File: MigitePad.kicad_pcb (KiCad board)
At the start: 2 copper layers, 139.7 x 134.1 mm, 74 parts, among them J1 OLED, J2 LED-Lily58-cache, SW1 SW_Push, SW2 Rotary_Encoder_Switch, U1 ProMicro

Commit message: Rewired Encoder
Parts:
- added H9: MountingHole, Lily58-footprint:HOLE_M2_TH, F.Cu at (142.1, 60.2)
- moved H6 9.22 mm to (116.7, 124.3)
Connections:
- D31 pad 1: ROW1 -> ROW0
- SW2 pad S2: COL6 -> COL3
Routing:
- net ROW0: track 90.8 -> 155.3 mm, vias 0 -> 5
- net COL3: track 115.7 -> 166.2 mm, vias 0 -> 3
- net COL6: track 171.5 -> 151.0 mm, vias 2 -> 1
- net ROW1: track 208.9 -> 206.2 mm

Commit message: Gerbers and final touches
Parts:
- added G***: LOGO, Logo:MigiteLogo, F.Cu at (132.5, 104.3)

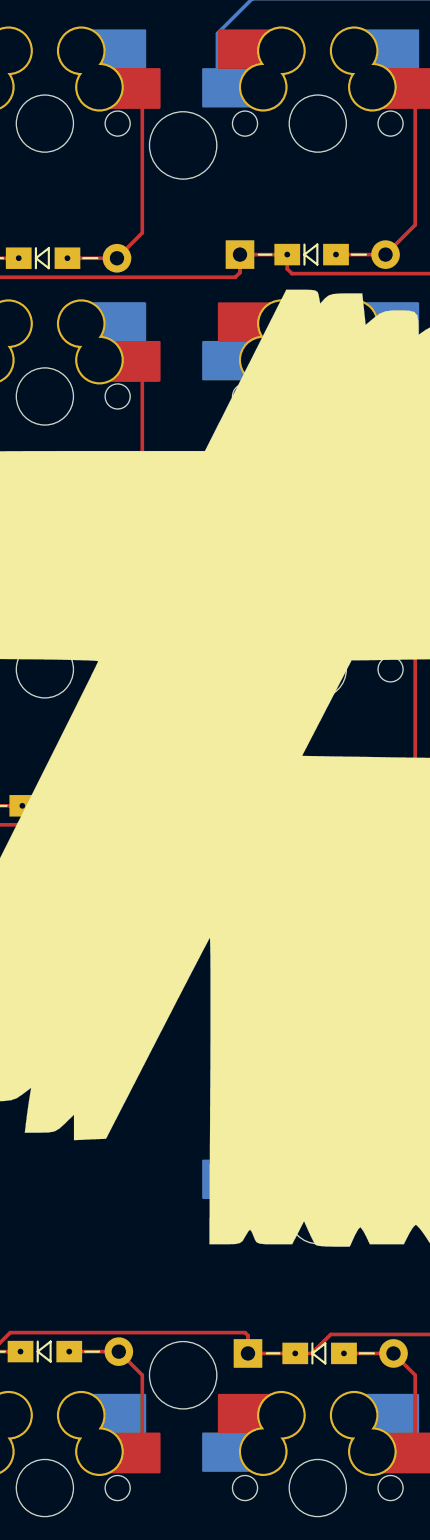
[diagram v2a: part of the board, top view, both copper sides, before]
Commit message: Corrected Col1 Trace
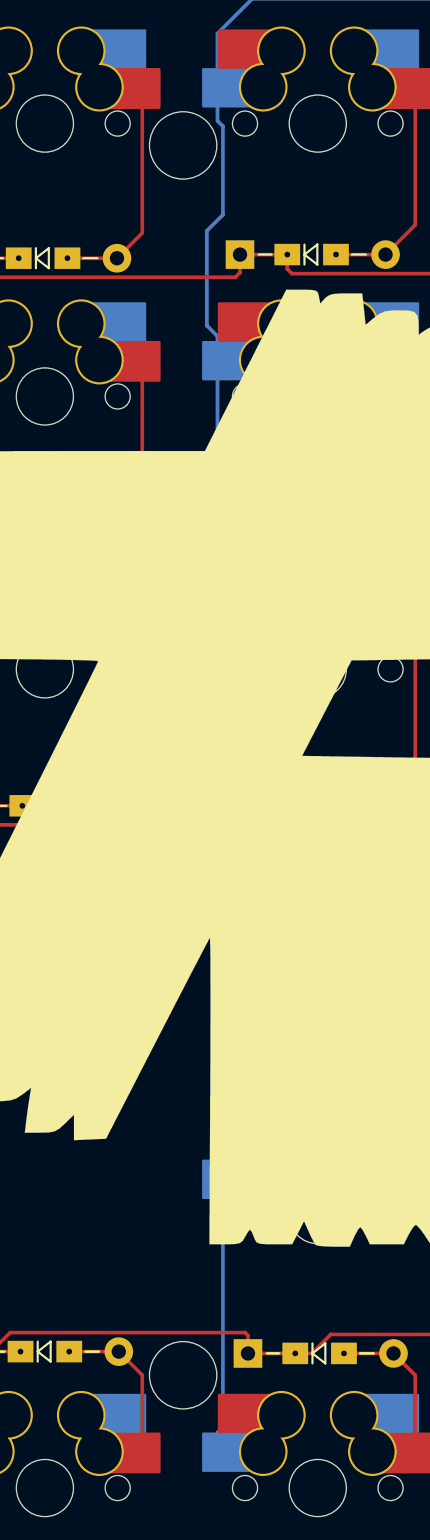
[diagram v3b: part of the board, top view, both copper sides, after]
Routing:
- net COL1: track 67.6 -> 164.1 mm
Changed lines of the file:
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@@
     (thickness 1.6)
     (drawings 22)
-    (tracks 552)
+    (tracks 568)
     (zones 0)
     (modules 76)
@@
     (35 F.Paste user hide)
     (36 B.SilkS user)
-    (37 F.SilkS user)
+    (37 F.SilkS user hide)
     (38 B.Mask user)
     (39 F.Mask user)
@@
   (segment (start 88.011 50.84402) (end 122.899047 50.84402) (width 0.254) (layer B.Cu) (net 37))
   (segment (start 122.899047 50.84402) (end 123.165 50.578066) (width 0.254) (layer B.Cu) (net 37))
+  (segment (start 85.583 57.063) (end 85.583 59.374742) (width 0.254) (layer B.Cu) (net 37))
+  (segment (start 85.962201 59.753943) (end 85.962201 65.929799) (width 0.254) (layer B.Cu) (net 37))
+  (segment (start 85.583 59.374742) (end 85.962201 59.753943) (width 0.254) (layer B.Cu) (net 37))
+  (segment (start 85.962201 65.929799) (end 84.836 67.056) (width 0.254) (layer B.Cu) (net 37))
+  (segment (start 84.836 67.056) (end 84.836 73.66) (width 0.254) (layer B.Cu) (net 37))
+  (segment (start 85.583 74.407) (end 85.583 76.113) (width 0.254) (layer B.Cu) (net 37))
+  (segment (start 84.836 73.66) (end 85.583 74.407) (width 0.254) (layer B.Cu) (net 37))
+  (segment (start 85.583 77.488) (end 85.583 95.163) (width 0.254) (layer B.Cu) (net 37))
+  (segment (start 85.583 76.113) (end 85.583 77.488) (width 0.254) (layer B.Cu) (net 37))
+  (segment (start 85.583 96.538) (end 85.583 133.263) (width 0.254) (layer B.Cu) (net 37))
+  (segment (start 85.583 95.163) (end 85.583 96.538) (width 0.254) (layer B.Cu) (net 37))
+  (segment (start 85.583 150.938) (end 85.583 152.313) (width 0.254) (layer B.Cu) (net 37))
+  (segment (start 85.962201 150.558799) (end 85.583 150.938) (width 0.254) (layer B.Cu) (net 37))
+  (segment (start 85.583 134.638) (end 85.962201 135.017201) (width 0.254) (layer B.Cu) (net 37))
+  (segment (start 85.962201 135.017201) (end 85.962201 150.558799) (width 0.254) (layer B.Cu) (net 37))
+  (segment (start 85.583 133.263) (end 85.583 134.638) (width 0.254) (layer B.Cu) (net 37))
   (segment (start 104.633 57.063) (end 104.633 152.313) (width 0.254) (layer B.Cu) (net 38))
   (segment (start 140.60173 40.27802) (end 144.81175 36.068) (width 0.254) (layer B.Cu) (net 38))

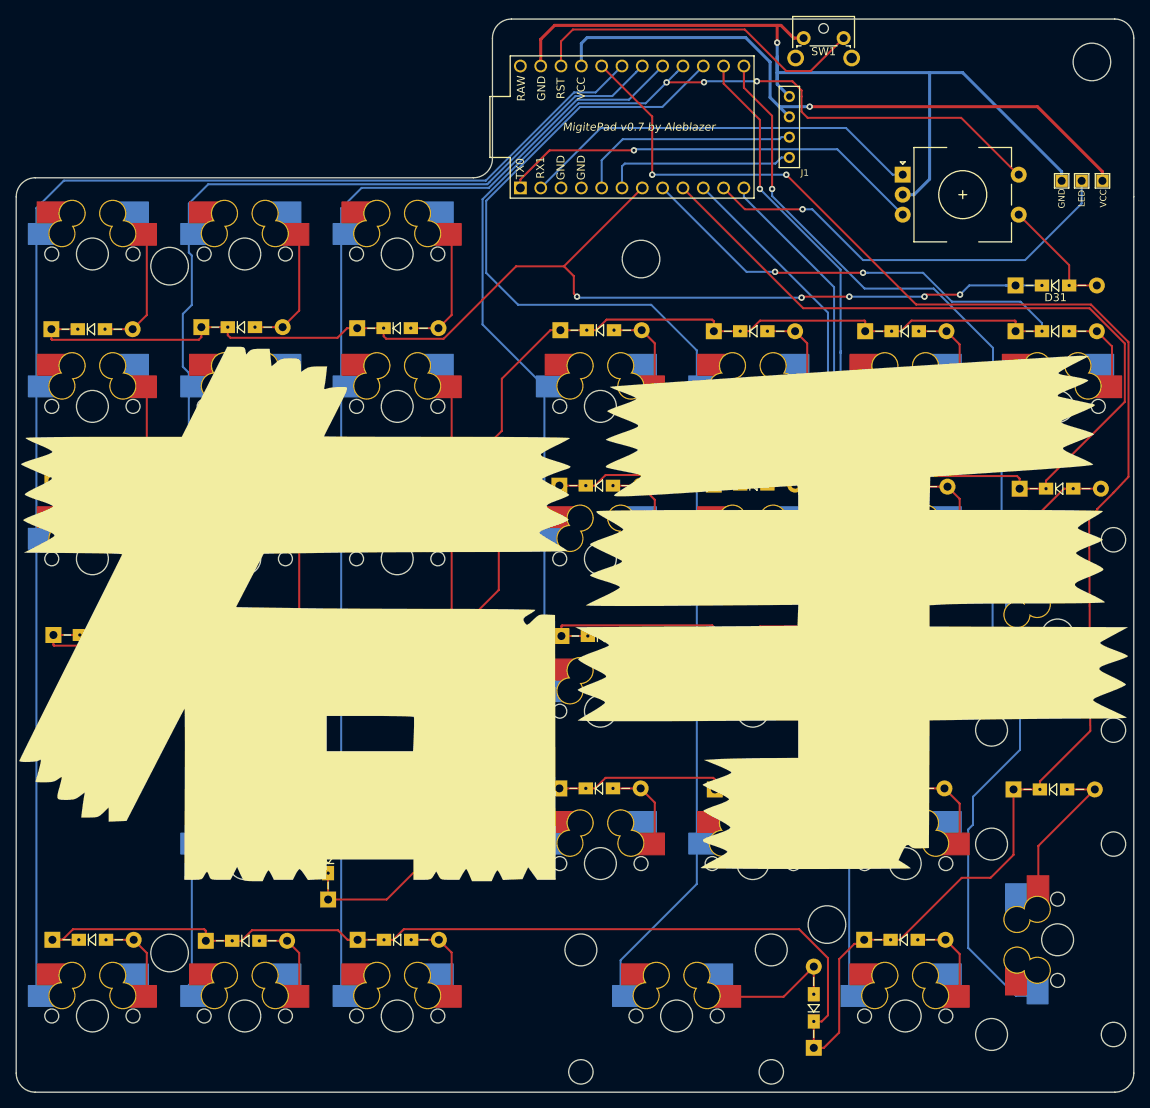
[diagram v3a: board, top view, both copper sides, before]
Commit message: Removed old Gerbers, fixed more traces
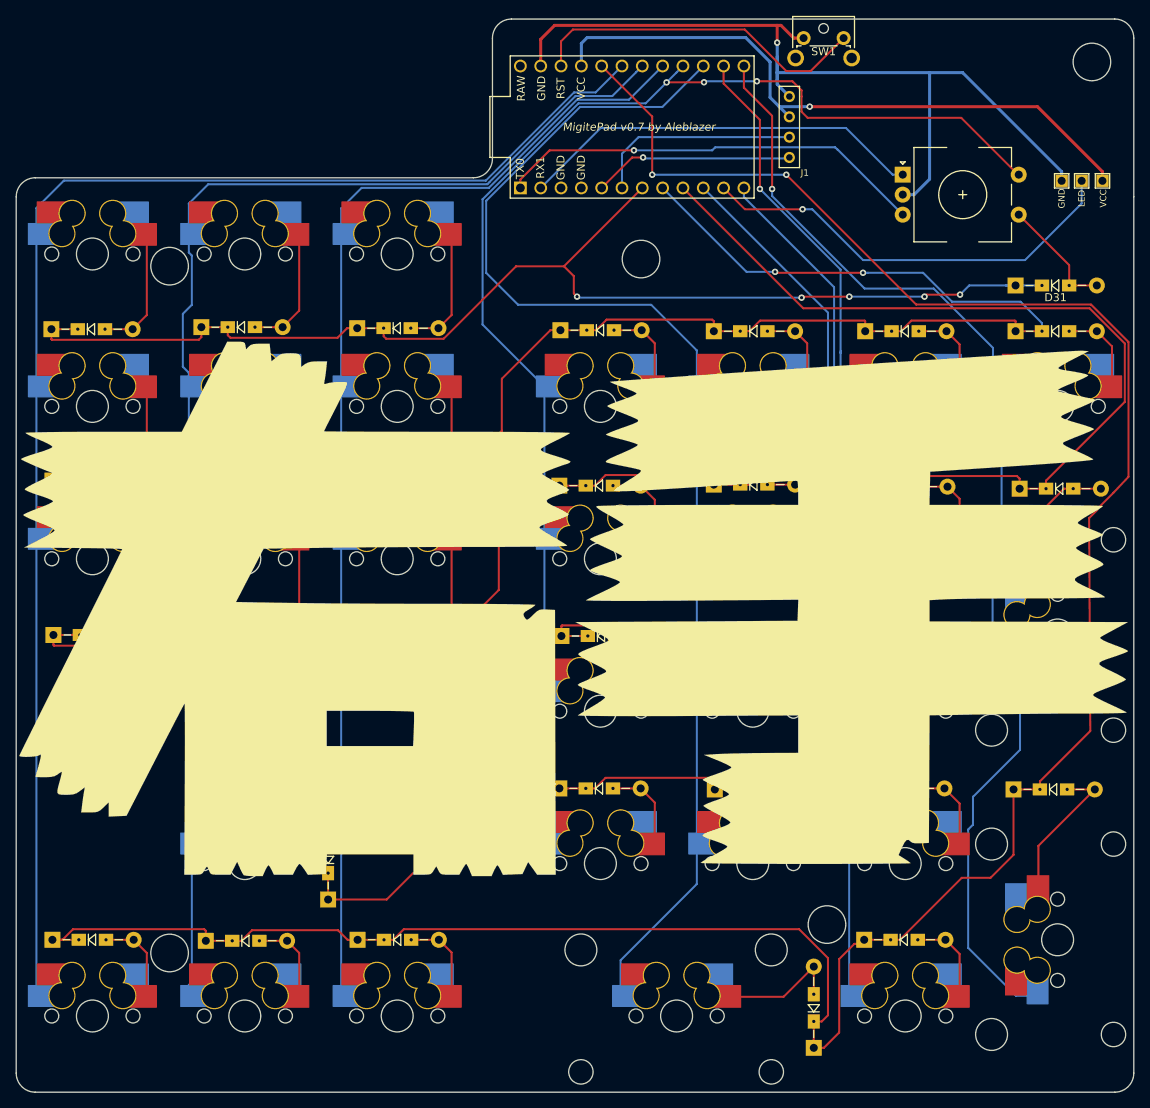
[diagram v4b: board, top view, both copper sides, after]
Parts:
- moved G*** 0.63 mm to (132.5, 103.6)
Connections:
- U1 pad 5: SCL -> SDA
- U1 pad 6: SDA -> SCL
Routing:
- net SCL: track 28.1 -> 26.1 mm
- net SDA: track 24.1 -> 25.2 mm, vias 0 -> 1
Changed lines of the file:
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@@
     (thickness 1.6)
     (drawings 22)
-    (tracks 568)
+    (tracks 572)
     (zones 0)
     (modules 76)
@@
     (35 F.Paste user hide)
     (36 B.SilkS user)
-    (37 F.SilkS user hide)
+    (37 F.SilkS user)
     (38 B.Mask user)
     (39 F.Mask user)
@@
   )
   (module Logo:MigiteLogo (layer F.Cu)
-    (at 132.461 104.267)
+    (at 132.461 103.632)
     (fp_text reference G*** (at 0 0) (layer F.SilkS) hide
       (effects (font (size 1.524 1.524) (thickness 0.3)))
@@
       (net 2 ROW0))
     (pad 6 thru_hole circle (at -1.27 7.62) (size 1.6 1.6) (drill 1.1) (layers *.Cu *.Mask F.SilkS)
-      (net 48 SDA))
-    (pad 5 thru_hole circle (at -3.81 7.62) (size 1.6 1.6) (drill 1.1) (layers *.Cu *.Mask F.SilkS)
       (net 47 SCL))
+    (pad 5 thru_hole circle (at -3.81 7.62) (size 1.6 1.6) (drill 1.1) (layers *.Cu *.Mask F.SilkS)
+      (net 48 SDA))
     (pad 4 thru_hole circle (at -6.35 7.62) (size 1.6 1.6) (drill 1.1) (layers *.Cu *.Mask F.SilkS)
       (net 45 GND))
@@
   (segment (start 191.663 41.148) (end 199.791 49.276) (width 0.381) (layer F.Cu) (net 46))
   (segment (start 163.195 41.148) (end 191.663 41.148) (width 0.381) (layer F.Cu) (net 46))
-  (segment (start 159.667172 44.958) (end 159.413172 45.212) (width 0.254) (layer B.Cu) (net 47))
-  (segment (start 160.655 44.958) (end 159.667172 44.958) (width 0.254) (layer B.Cu) (net 47))
-  (segment (start 159.413172 45.212) (end 139.827 45.212) (width 0.254) (layer B.Cu) (net 47))
-  (segment (start 137.19175 47.84725) (end 137.19175 51.308) (width 0.254) (layer B.Cu) (net 47))
-  (segment (start 139.827 45.212) (end 137.19175 47.84725) (width 0.254) (layer B.Cu) (net 47))
-  (segment (start 140.081 48.26) (end 139.73175 48.60925) (width 0.254) (layer B.Cu) (net 48))
-  (segment (start 158.905172 48.26) (end 140.081 48.26) (width 0.254) (layer B.Cu) (net 48))
-  (segment (start 160.655 47.498) (end 159.667172 47.498) (width 0.254) (layer B.Cu) (net 48))
-  (segment (start 139.73175 48.60925) (end 139.73175 51.308) (width 0.254) (layer B.Cu) (net 48))
-  (segment (start 159.667172 47.498) (end 158.905172 48.26) (width 0.254) (layer B.Cu) (net 48))
+  (segment (start 139.73175 47.025288) (end 139.73175 50.17663) (width 0.254) (layer B.Cu) (net 47))
+  (segment (start 141.799038 44.958) (end 139.73175 47.025288) (width 0.254) (layer B.Cu) (net 47))
+  (segment (start 139.73175 50.17663) (end 139.73175 51.308) (width 0.254) (layer B.Cu) (net 47))
+  (segment (start 160.655 44.958) (end 141.799038 44.958) (width 0.254) (layer B.Cu) (net 47))
+  (segment (start 160.655 47.498) (end 160.655 47.625) (width 0.254) (layer B.Cu) (net 48))
+  (segment (start 160.655 47.625) (end 142.494 47.625) (width 0.254) (layer B.Cu) (net 48))
+  (via (at 142.367 47.498) (size 0.8) (drill 0.4) (layers F.Cu B.Cu) (net 48))
+  (segment (start 142.494 47.625) (end 142.367 47.498) (width 0.254) (layer B.Cu) (net 48))
+  (segment (start 141.00175 47.498) (end 137.19175 51.308) (width 0.254) (layer F.Cu) (net 48))
+  (segment (start 142.367 47.498) (end 141.00175 47.498) (width 0.254) (layer F.Cu) (net 48))
   (segment (start 132.11175 32.98825) (end 132.11175 36.068) (width 0.254) (layer F.Cu) (net 49))
   (segment (start 163.3055 36.703) (end 160.274 36.703) (width 0.254) (layer F.Cu) (net 49))
@@
   (segment (start 199.089 63.49746) (end 195.63154 63.49746) (width 0.254) (layer F.Cu) (net 51))
   (segment (start 195.629 60.953) (end 189.325 54.649) (width 0.254) (layer F.Cu) (net 51))
-  (segment (start 173.571 49.649) (end 167.737 43.815) (width 0.254) (layer B.Cu) (net 52))
-  (segment (start 174.825 49.649) (end 173.571 49.649) (width 0.254) (layer B.Cu) (net 52))
-  (segment (start 137.06475 43.815) (end 129.57175 51.308) (width 0.254) (layer B.Cu) (net 52))
-  (segment (start 167.737 43.815) (end 137.06475 43.815) (width 0.254) (layer B.Cu) (net 52))
+  (segment (start 167.737 43.815) (end 173.571 49.649) (width 0.254) (layer B.Cu) (net 52))
+  (segment (start 137.06475 43.815) (end 167.737 43.815) (width 0.254) (layer B.Cu) (net 52))
+  (segment (start 173.571 49.649) (end 174.825 49.649) (width 0.254) (layer B.Cu) (net 52))
+  (segment (start 129.57175 51.308) (end 137.06475 43.815) (width 0.254) (layer B.Cu) (net 52))
   (via (at 141.224 46.609) (size 0.8) (drill 0.4) (layers F.Cu B.Cu) (net 53))
   (segment (start 174.825 54.649) (end 166.648499 46.472499) (width 0.254) (layer B.Cu) (net 53))
   (segment (start 141.360501 46.472499) (end 141.224 46.609) (width 0.254) (layer B.Cu) (net 53))
-  (segment (start 166.648499 46.472499) (end 141.360501 46.472499) (width 0.254) (layer B.Cu) (net 53))
   (segment (start 127.03175 50.254) (end 127.03175 51.308) (width 0.254) (layer F.Cu) (net 53))
   (segment (start 130.67675 46.609) (end 127.03175 50.254) (width 0.254) (layer F.Cu) (net 53))
   (segment (start 141.224 46.609) (end 130.67675 46.609) (width 0.254) (layer F.Cu) (net 53))
+  (segment (start 166.648499 46.472499) (end 166.614499 46.472499) (width 0.254) (layer B.Cu) (net 53))
+  (segment (start 166.614499 46.472499) (end 166.37 46.228) (width 0.254) (layer B.Cu) (net 53))
+  (segment (start 166.37 46.228) (end 151.384 46.228) (width 0.254) (layer B.Cu) (net 53))
+  (segment (start 151.003 46.609) (end 141.224 46.609) (width 0.254) (layer B.Cu) (net 53))
+  (segment (start 151.384 46.228) (end 151.003 46.609) (width 0.254) (layer B.Cu) (net 53))
 )

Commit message: Updated Gerbers and README.md
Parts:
- added G***: LOGO, Logo:MigiteLogoBack, B.Cu at (133.5, 104.5)
